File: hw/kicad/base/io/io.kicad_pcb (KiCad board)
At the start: 2 copper layers, 50 x 50 mm, 13 parts, among them J1 SPI, J10 Conn_02x20_Odd_Even, J11 ADC 2, J12 UART1, J13 Conn_02x20_Odd_Even, J2 PWM, J3 UART2, J4 I2C, J5 PWM, J6 CAN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

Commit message: Pindar v1.0
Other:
- board text added: "Pindar v1.0 Type BASE io v1.0"
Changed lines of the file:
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@@
   (gr_circle locked (center 75.72 73.22) (end 76.72 73.22)
     (stroke (width 0.15) (type default)) (fill none) (layer "User.1"))
+  (gr_text "Pindar v1.0 \nType BASE\nio v1.0" (at 54.1808 70.8832) (layer "F.SilkS")
+    (effects (font (size 1 1) (thickness 0.15)) (justify left bottom))
+  )
   (segment (start 66.750266 60.5962) (end 57.5082 60.5962) (width 0.2032) (layer "F.Cu") (net 1))
   (segment (start 57.0726 61.0318) (end 57.0726 62.1652) (width 0.2032) (layer "F.Cu") (net 1))

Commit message: 更新read me
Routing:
- net /+5V: track 3.76 -> 11.6 mm
- net +3.3V: track 205.7 -> 209.6 mm
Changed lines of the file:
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@@
   (segment (start 68.7604 40.4286) (end 79.1236 40.4286) (width 0.2032) (layer "F.Cu") (net 1))
   (segment (start 79.533532 50.4108) (end 79.533532 42.0296) (width 0.2032) (layer "F.Cu") (net 1))
-  (segment (start 80.165 71.27) (end 80.165 75.17) (width 0.381) (layer "F.Cu") (net 1))
   (segment (start 90.7852 57.4944) (end 88.293 59.9866) (width 0.2032) (layer "F.Cu") (net 1))
   (segment (start 68.293466 40.895534) (end 68.7604 40.4286) (width 0.2032) (layer "F.Cu") (net 1))
@@
   (segment (start 68.319266 52.068) (end 68.281866 52.0306) (width 0.2032) (layer "F.Cu") (net 1))
   (segment (start 79.540132 42.023) (end 79.540132 41.028068) (width 0.2032) (layer "F.Cu") (net 1))
+  (segment (start 80.165 71.27) (end 80.165 75.17) (width 0.762) (layer "F.Cu") (net 1))
   (segment (start 90.8076 52.0082) (end 90.7852 52.0306) (width 0.2032) (layer "F.Cu") (net 1))
   (segment (start 68.281866 52.0306) (end 68.281866 50.508334) (width 0.2032) (layer "F.Cu") (net 1))
@@
   (segment (start 57.051 74.49) (end 59.972 77.411) (width 0.381) (layer "B.Cu") (net 1))
   (segment (start 79.457332 50.487) (end 79.533532 50.4108) (width 0.2032) (layer "B.Cu") (net 1))
+  (segment (start 80.165 71.27) (end 80.165 75.17) (width 0.762) (layer "B.Cu") (net 1))
   (via (at 77.0662 43.7814) (size 0.508) (drill 0.254) (layers "F.Cu" "B.Cu") (net 2))
   (via (at 74.831 55.567) (size 0.508) (drill 0.254) (layers "F.Cu" "B.Cu") (net 2))
@@
   (via (at 78.8924 75.1332) (size 0.508) (drill 0.254) (layers "F.Cu" "B.Cu") (net 27))
   (via (at 78.8924 74.3712) (size 0.508) (drill 0.254) (layers "F.Cu" "B.Cu") (net 27))
+  (segment (start 81.435 71.27) (end 81.435 75.17) (width 0.762) (layer "F.Cu") (net 28))
   (segment (start 81.4324 71.374) (end 81.4324 75.1332) (width 0.381) (layer "F.Cu") (net 28))
   (via (at 81.4324 75.1332) (size 0.508) (drill 0.254) (layers "F.Cu" "B.Cu") (net 28))
@@
   (via (at 81.4324 71.374) (size 0.508) (drill 0.254) (layers "F.Cu" "B.Cu") (net 28))
   (via (at 81.4324 72.136) (size 0.508) (drill 0.254) (layers "F.Cu" "B.Cu") (net 28))
+  (segment (start 81.435 71.27) (end 81.435 75.17) (width 0.762) (layer "B.Cu") (net 28))
   (via (at 85.1916 73.2536) (size 0.508) (drill 0.254) (layers "F.Cu" "B.Cu") (free) (net 29))
   (via (at 83.9724 75.184) (size 0.508) (drill 0.254) (layers "F.Cu" "B.Cu") (net 29))

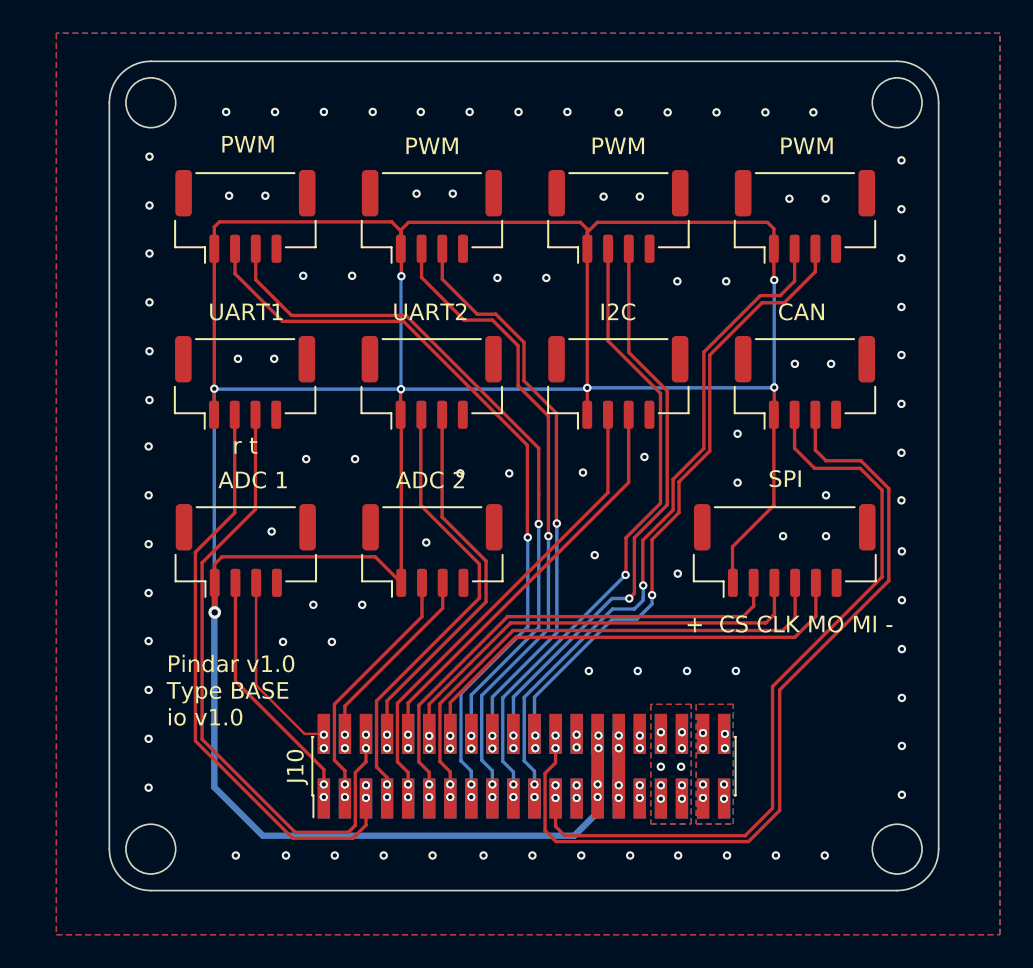
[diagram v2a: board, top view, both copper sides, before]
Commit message: 新增陀螺仪小板子
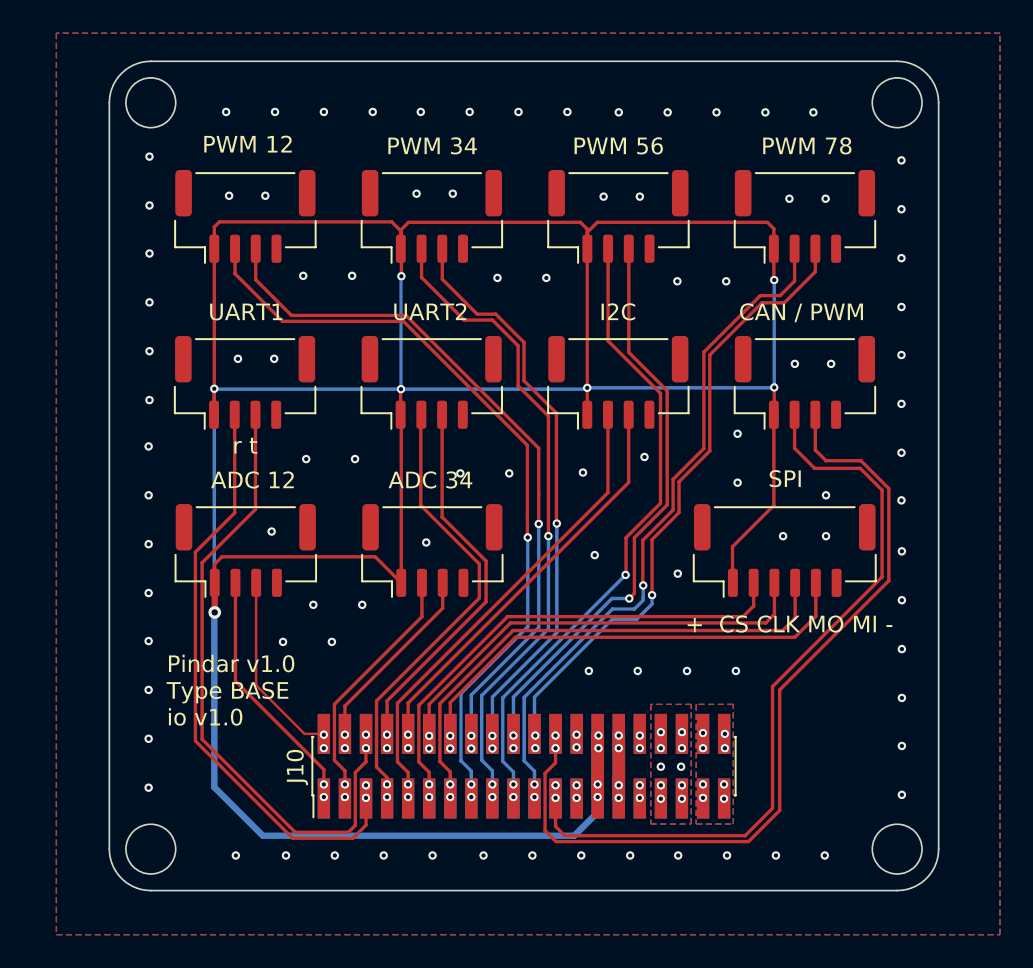
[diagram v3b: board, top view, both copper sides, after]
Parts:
- J11: value ADC 2 -> ADC 34
- J2: value PWM -> PWM 12
- J5: value PWM -> PWM 34
- J6: value CAN -> CAN / PWM
- J7: value PWM -> PWM 56
- J8: value PWM -> PWM 78
- J9: value ADC 1 -> ADC 12
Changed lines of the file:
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@@
         (effects (font (size 1 1) (thickness 0.15)))
     )
-    (fp_text value "PWM" (at 0.1606 -4.3164) (layer "F.SilkS")
+    (fp_text value "PWM 12" (at 0.1606 -4.3164) (layer "F.SilkS")
         (effects (font (size 1 1) (thickness 0.15)))
     )
@@
         (effects (font (size 1 1) (thickness 0.15)))
     )
-    (fp_text value "PWM" (at 0.013934 -4.2164) (layer "F.SilkS")
+    (fp_text value "PWM 34" (at 0.013934 -4.2164) (layer "F.SilkS")
         (effects (font (size 1 1) (thickness 0.15)))
     )
@@
         (effects (font (size 1 1) (thickness 0.15)))
     )
-    (fp_text value "ADC 2" (at -0.081066 -4.2164) (layer "F.SilkS")
+    (fp_text value "ADC 34" (at -0.081066 -4.2164) (layer "F.SilkS")
         (effects (font (size 1 1) (thickness 0.15)))
     )
@@
         (effects (font (size 1 1) (thickness 0.15)))
     )
-    (fp_text value "PWM" (at -0.0044 -4.2164) (layer "F.SilkS")
+    (fp_text value "PWM 56" (at -0.0044 -4.2164) (layer "F.SilkS")
         (effects (font (size 1 1) (thickness 0.15)))
     )
@@
         (effects (font (size 1 1) (thickness 0.15)))
     )
-    (fp_text value "PWM" (at 0.1206 -4.2164) (layer "F.SilkS")
+    (fp_text value "PWM 78" (at 0.1206 -4.2164) (layer "F.SilkS")
         (effects (font (size 1 1) (thickness 0.15)))
     )
@@
         (effects (font (size 1 1) (thickness 0.15)))
     )
-    (fp_text value "CAN" (at -0.1794 -4.2164) (layer "F.SilkS")
+    (fp_text value "CAN / PWM" (at -0.1794 -4.2164) (layer "F.SilkS")
         (effects (font (size 1 1) (thickness 0.15)))
     )
@@
         (effects (font (size 1 1) (thickness 0.15)))
     )
-    (fp_text value "ADC 1" (at 0.4656 -4.2164) (layer "F.SilkS")
-        (effects (font (size 1 1) (thickness 0.15)))
-    )
+    (fp_text value "ADC 12" (at 0.4656 -4.2164) (layer "F.SilkS")
+        (effects (font (size 1 1) (thickness 0.15)))
+    )

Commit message: 第二次打样的整改；dc motor改成了三路 io不够做不了四路；
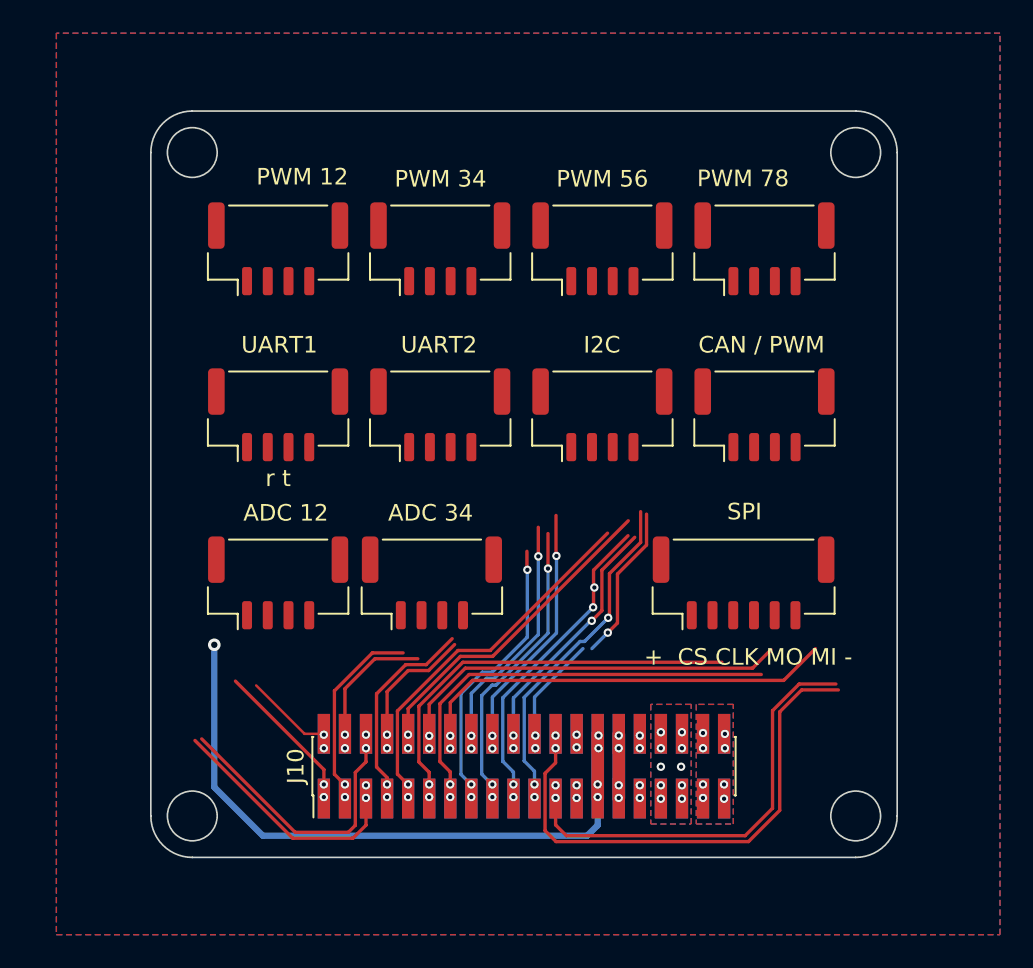
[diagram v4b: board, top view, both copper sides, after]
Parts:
- moved J1 3.16 mm to (89.0, 62.2)
- moved J8 3.13 mm to (90.2, 42.0)
- moved J6 3.12 mm to (90.2, 52.0)
- moved J12 2.79 mm to (60.9, 52.0)
- moved J2 2.78 mm to (60.9, 42.0)
- moved J9 2.76 mm to (60.9, 62.2)
- moved J7 2.18 mm to (80.4, 42.0)
- moved J4 2.18 mm to (80.4, 52.0)
- moved J3 2.02 mm to (70.7, 52.0)
- moved J5 2.02 mm to (70.7, 42.0)
- moved J11 1.95 mm to (70.2, 62.2)
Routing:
- net +3.3V: track 209.6 -> 42.6 mm, vias 11 -> 5
- net /PWM_8: track 37.9 -> 6.35 mm, vias 3 -> 2
- net /PWM_1: track 46.7 -> 17.2 mm
- net /PWM_2: track 42.2 -> 14.5 mm
- net /PWM_3: track 39.2 -> 18.0 mm
- net /UART1_TX: track 38.4 -> 17.5 mm
- net /UART1_RX: track 35.3 -> 14.7 mm
- net /CAN_H: track 45.9 -> 26.0 mm
- net /PWM_6: track 34.8 -> 15.0 mm
- net /CAN_L: track 51.0 -> 31.3 mm
- net /PWM_4: track 34.4 -> 14.8 mm
- net /PWM_5: track 38.7 -> 19.2 mm, vias 3 -> 4
- net /UART2_TX: track 22.8 -> 7.79 mm
- net /UART2_RX: track 27.4 -> 12.4 mm
- net /PWM_7: track 41.6 -> 30.0 mm, vias 3 -> 4
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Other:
- board size 50 x 50 mm -> 45 x 45 mm
- board text removed: "Pindar v1.0 Type BASE io v1.0"

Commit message: 更换接口线序
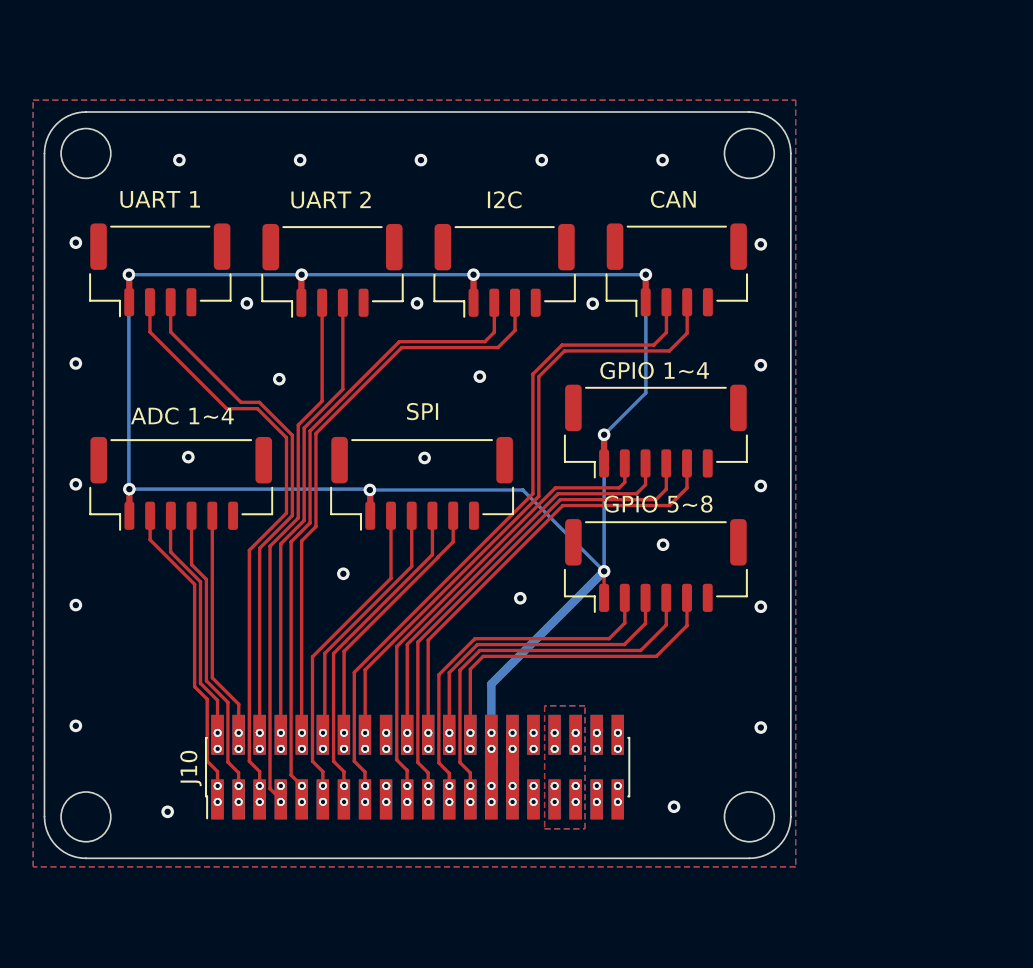
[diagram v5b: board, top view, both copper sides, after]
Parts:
- removed J11: ADC 34, Connector_JST:JST_GH_BM04B-GHS-TBT_1x04-1MP_P1.25mm_Vertical
- removed J12: UART1, Connector_JST:JST_GH_BM04B-GHS-TBT_1x04-1MP_P1.25mm_Vertical
- removed J9: ADC 12, Connector_JST:JST_GH_BM04B-GHS-TBT_1x04-1MP_P1.25mm_Vertical
- J2: value PWM 12 -> GPIO 1~4; footprint Connector_JST:JST_GH_BM04B-GHS-TBT_1x04-1MP_P1.25mm_Vertical -> Connector_JST:JST_GH_BM06B-GHS-TBT_1x06-1MP_P1.25mm_Vertical
- J3: value UART2 -> UART 2
- J5: value PWM 34 -> GPIO 5~8; footprint Connector_JST:JST_GH_BM04B-GHS-TBT_1x04-1MP_P1.25mm_Vertical -> Connector_JST:JST_GH_BM06B-GHS-TBT_1x06-1MP_P1.25mm_Vertical
- J6: value CAN / PWM -> CAN
- J7: value PWM 56 -> UART 1
- J8: value PWM 78 -> ADC 1~4; footprint Connector_JST:JST_GH_BM04B-GHS-TBT_1x04-1MP_P1.25mm_Vertical -> Connector_JST:JST_GH_BM06B-GHS-TBT_1x06-1MP_P1.25mm_Vertical
- moved J8 37.9 mm to (55.1, 56.2)
- moved J7 26.7 mm to (53.8, 43.3)
- moved J2 25.3 mm to (83.7, 53.0)
- moved J5 23.1 mm to (83.7, 61.1)
- moved J1 20.3 mm to (69.6, 56.2)
- moved J3 10.9 mm to (64.2, 43.3)
- moved J4 10.5 mm to (74.6, 43.3)
- moved J6 10.2 mm to (84.9, 43.3)
- moved J10 6.41 mm to (69.3, 73.3)
- moved J13 6.41 mm to (69.3, 73.3)
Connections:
- J1 pad MP: (no net) -> GND
- J10 pad 15: /PWM_1 -> /CAN_H
- J10 pad 16: /PWM_2 -> /CAN_L
- J10 pad 17: /PWM_3 -> /USB+
- J10 pad 18: /PWM_4 -> /USB-
- J10 pad 19: /PWM_5 -> /GPIO_1
- J10 pad 20: /PWM_6 -> /GPIO_2
- J10 pad 21: /PWM_7 -> /GPIO_3
- J10 pad 22: /PWM_8 -> /GPIO_4
- J10 pad 23: /CAN_H -> /GPIO_5
- J10 pad 24: /CAN_L -> /GPIO_6
- J10 pad 25: /USB+ -> /GPIO_7
- J10 pad 26: /USB- -> /GPIO_8
- J13 pad 15: /PWM_2 -> /CAN_L
- J13 pad 16: /PWM_1 -> /CAN_H
- J13 pad 17: /PWM_4 -> /USB-
- J13 pad 18: /PWM_3 -> /USB+
- J13 pad 19: /PWM_6 -> /GPIO_2
- J13 pad 20: /PWM_5 -> /GPIO_1
- J13 pad 21: /PWM_8 -> /GPIO_4
- J13 pad 22: /PWM_7 -> /GPIO_3
- J13 pad 23: /CAN_L -> /GPIO_6
- J13 pad 24: /CAN_H -> /GPIO_5
- J13 pad 25: /USB- -> /GPIO_8
- J13 pad 26: /USB+ -> /GPIO_7
- J2 pad 2: /PWM_1 -> /GPIO_1
- J2 pad 3: /PWM_2 -> /GPIO_2
- J2 pad 4: GND -> /GPIO_3
- J2 pad MP: (no net) -> GND
- J3 pad MP: (no net) -> GND
- J4 pad MP: (no net) -> GND
- J5 pad 2: /PWM_3 -> /GPIO_5
- J5 pad 3: /PWM_4 -> /GPIO_6
- J5 pad 4: GND -> /GPIO_7
- J5 pad MP: (no net) -> GND
- J6 pad MP: (no net) -> GND
- J7 pad 2: /PWM_5 -> /UART1_RX
- J7 pad 3: /PWM_6 -> /UART1_TX
- J7 pad MP: (no net) -> GND
- J8 pad 2: /PWM_7 -> /ADC_1
- J8 pad 3: /PWM_8 -> /ADC_2
- J8 pad 4: GND -> /ADC_3
- J8 pad MP: (no net) -> GND
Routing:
- net +3.3V: track 42.6 -> 127.4 mm, vias 5 -> 12
- net /GPIO_3: track 0.00 -> 30.1 mm, vias 0 -> 2
- net /PWM_7: track 30.0 -> 0.00 mm, vias 4 -> 0
- net /GPIO_1: track 0.00 -> 28.5 mm, vias 0 -> 2
- net /GPIO_4: track 0.00 -> 26.6 mm, vias 0 -> 2
- net /GPIO_2: track 0.00 -> 25.0 mm, vias 0 -> 2
- net /GPIO_7: track 0.00 -> 23.2 mm, vias 0 -> 2
- net /GPIO_5: track 0.00 -> 21.8 mm, vias 0 -> 2
- net /UART1_RX: track 14.7 -> 35.7 mm
- net /UART2_TX: track 7.79 -> 27.6 mm
- net /GPIO_8: track 0.00 -> 19.8 mm, vias 0 -> 2
- net /PWM_5: track 19.2 -> 0.00 mm, vias 4 -> 0
- net /UART2_RX: track 12.4 -> 31.5 mm
- net /GPIO_6: track 0.00 -> 18.3 mm, vias 0 -> 2
- net /PWM_3: track 18.0 -> 0.00 mm, vias 3 -> 0
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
